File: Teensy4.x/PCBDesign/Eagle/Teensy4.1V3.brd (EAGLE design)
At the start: 55.9 x 66 mm, 8 parts

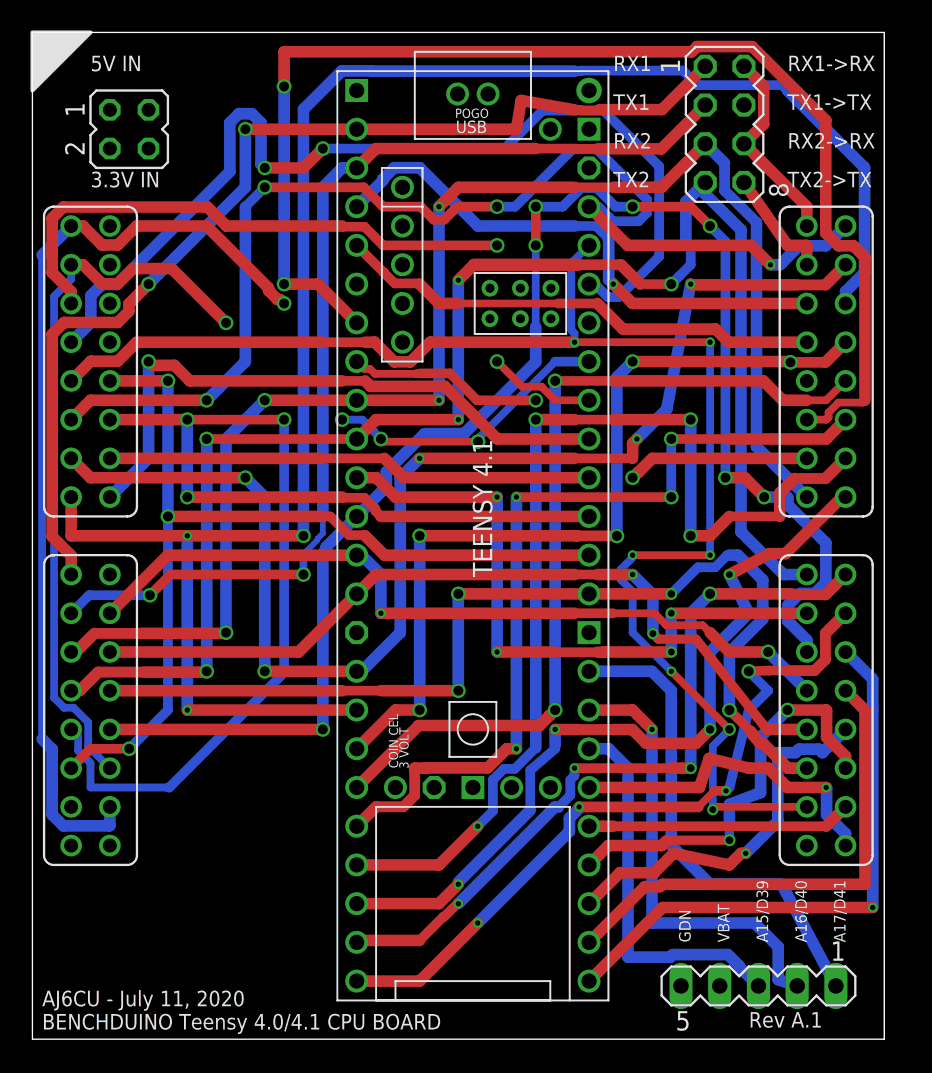
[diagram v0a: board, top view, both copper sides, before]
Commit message: Updated Teensy to correct power error
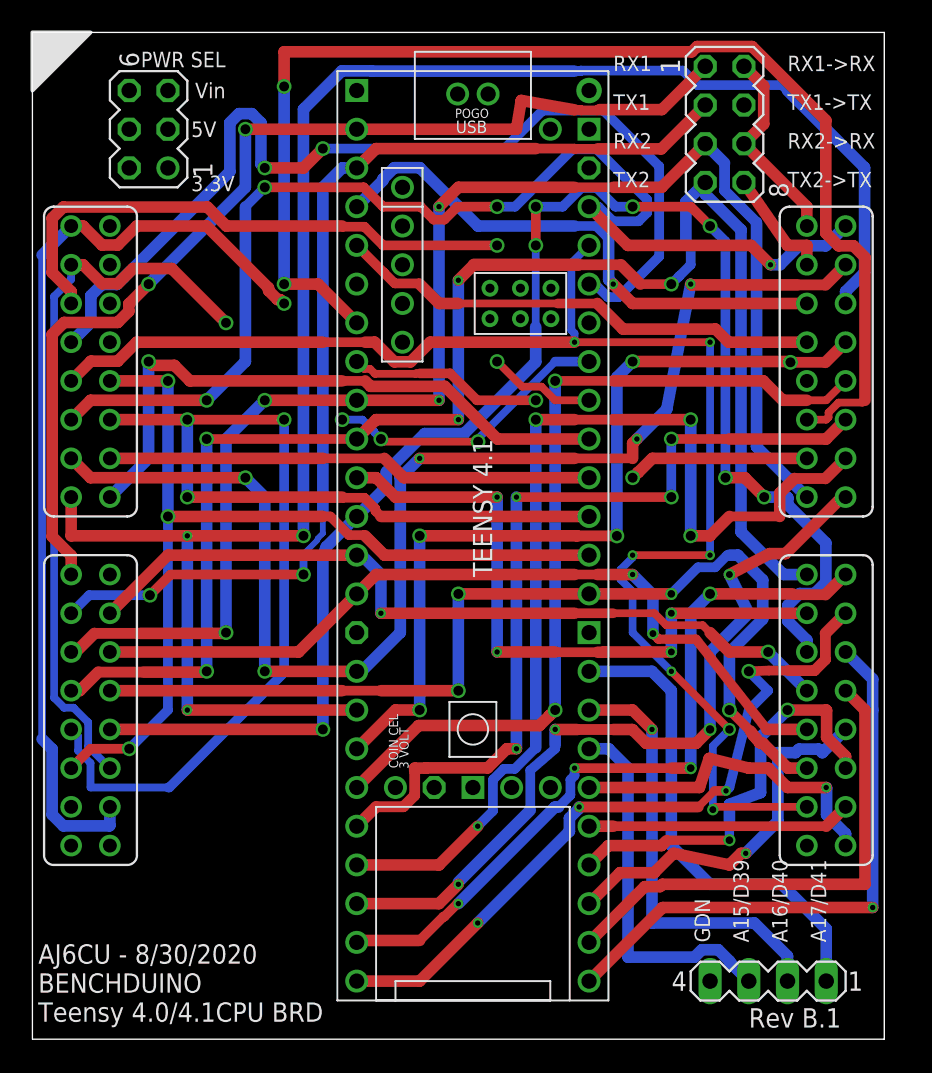
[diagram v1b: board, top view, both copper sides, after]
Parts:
- removed JP1: (no value), jumper:JP2Q
- removed SV2: (no value), con-lstb:MA05-1
- added SV3: (no value), con-lstb:MA03-2
- added SV4: (no value), con-lstb:MA04-1
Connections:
- removed net +5V(NC): SV48.14
- removed net VBAT: SV2.4, U$1.VBAT
- new net +5V: SV3.4, SV48.14
- net 3V3_IN: now also SV3.2; no longer JP1.3
- net 3V3_IN-TEENSY: now also SV3.1; no longer JP1.4
- net A15(D39): now also SV4.3; no longer SV2.3
- net A16(D40): now also SV4.2; no longer SV2.2
- net A17(D41): now also SV4.1; no longer SV2.1
- net DGND: now also SV4.4; no longer SV2.5
- net VIN: now also SV3.6; no longer JP1.1
- net VIN-TEENSY: now also SV3.3, SV3.5; no longer JP1.2
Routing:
- net VBAT: track 33.7 -> 0.00 mm
- net +5V: track 0.00 -> 10.5 mm
- net VIN: track 8.65 -> 11.2 mm
- net 3V3_IN-TEENSY: track 37.4 -> 35.6 mm
- net DGND: track 138.0 -> 139.8 mm
- net 3V3_IN: track 11.2 -> 10.2 mm
- net A16(D40): track 29.7 -> 28.8 mm
- net VIN-TEENSY: track 31.2 -> 32.0 mm
- net A15(D39): track 25.0 -> 24.5 mm
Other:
- board text added: "3.3V"
- board text added: "5V"
- board text added: "AJ6CU - 8/30/2020 BENCHDUINO Teensy 4.0/4.1CPU BRD"
- board text added: "PWR SEL"
- board text added: "Rev B.1"
- board text added: "Vin"
- board text removed: "3.3V IN"
- board text removed: "5V IN"
- board text removed: "AJ6CU - July 11, 2020 BENCHDUINO Teensy 4.0/4.1 CPU BOARD"
- board text removed: "Rev A.1"
- board text removed: "VBAT"
